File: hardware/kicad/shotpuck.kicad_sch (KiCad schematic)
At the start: 27 parts, among them J1 Magnetic pogo 2P (female), J2 TC2030-NL, Q1 DMN63D8LDW, U1 MDBT50Q-512K, U2 LIS2DE12TR, U3 MCP73831T-2ACI/OT

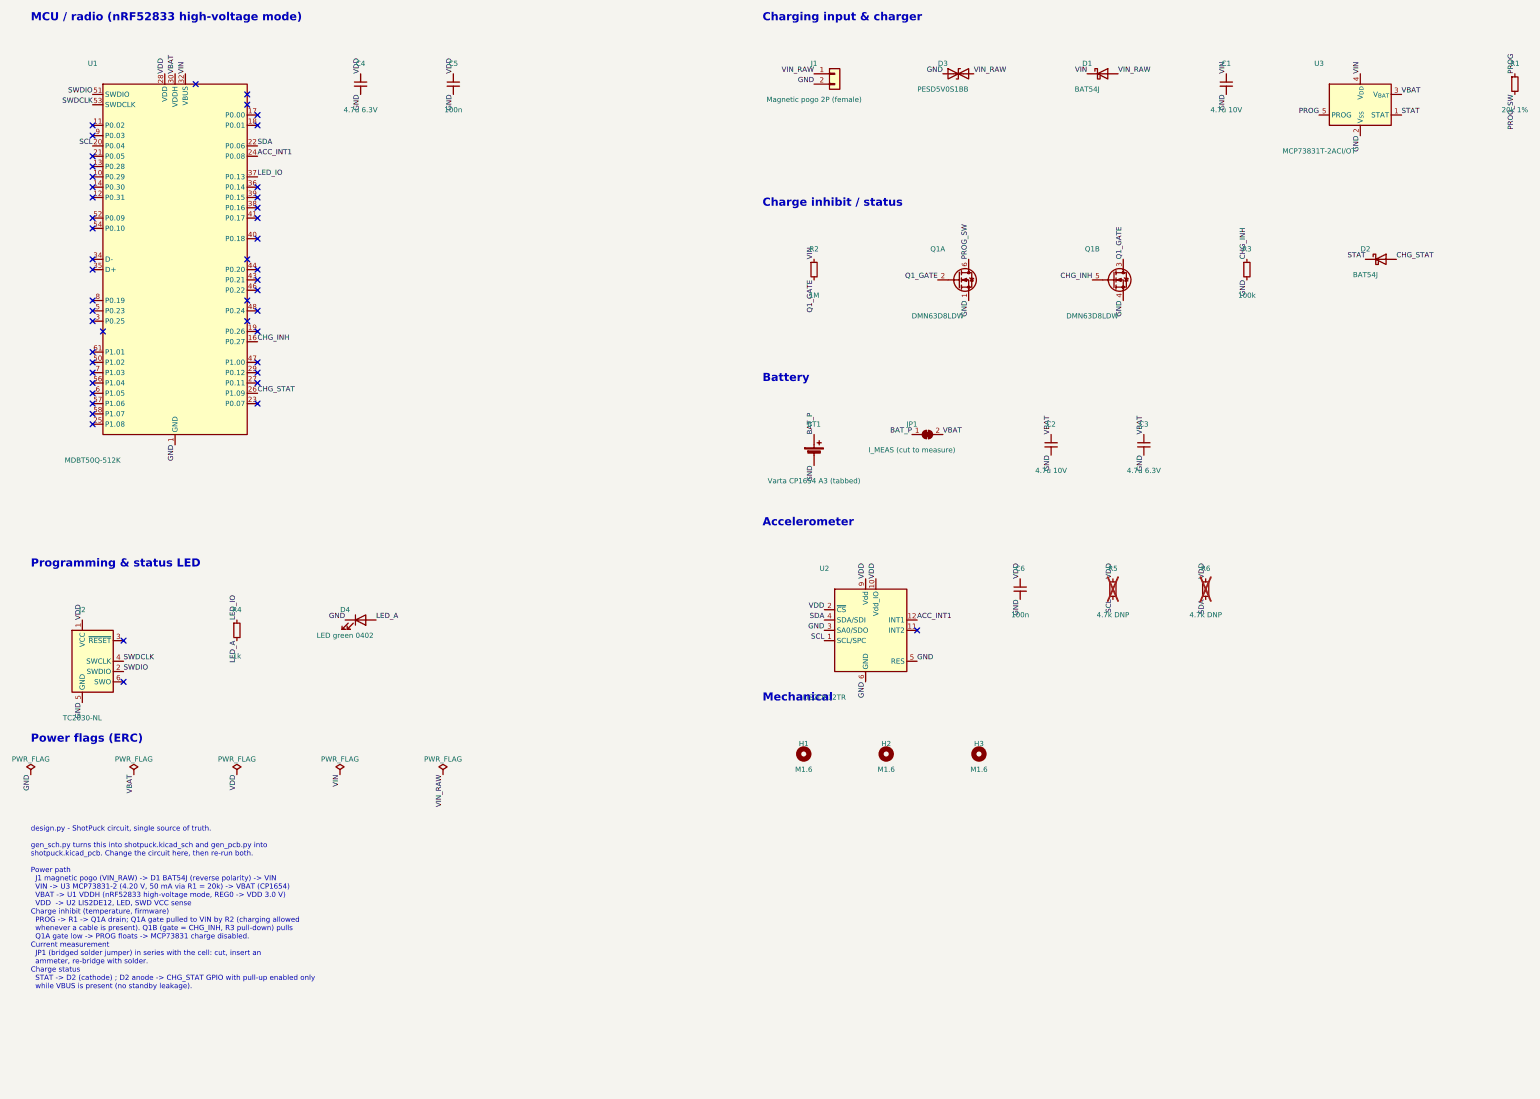
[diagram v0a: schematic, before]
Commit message: Update ShotPuck to v0.2 design package
Enhancements include the integration of the LSM6DSO32 IMU, which replaces the LIS2DE12 accelerometer, allowing for 6-axis motion capture. The new CAPTURE characteristic streams raw data around each shot, improving performance metrics. The firmware and simulation have been updated to support these changes, including adjustments to the BLE protocol (v2) for better data handling. Additionally, the toolchain has been migrated to a native Windows environment for development.

Key changes:
- Updated deliverable status to v0.2.
- Added capture functionality for bow motion.
- Adjusted simulation and validation processes to reflect new hardware capabilities.
- Enhanced documentation to include new features and user requirements.

Co-Authored-By: Claude Opus 5.5 <noreply@anthropic.com>
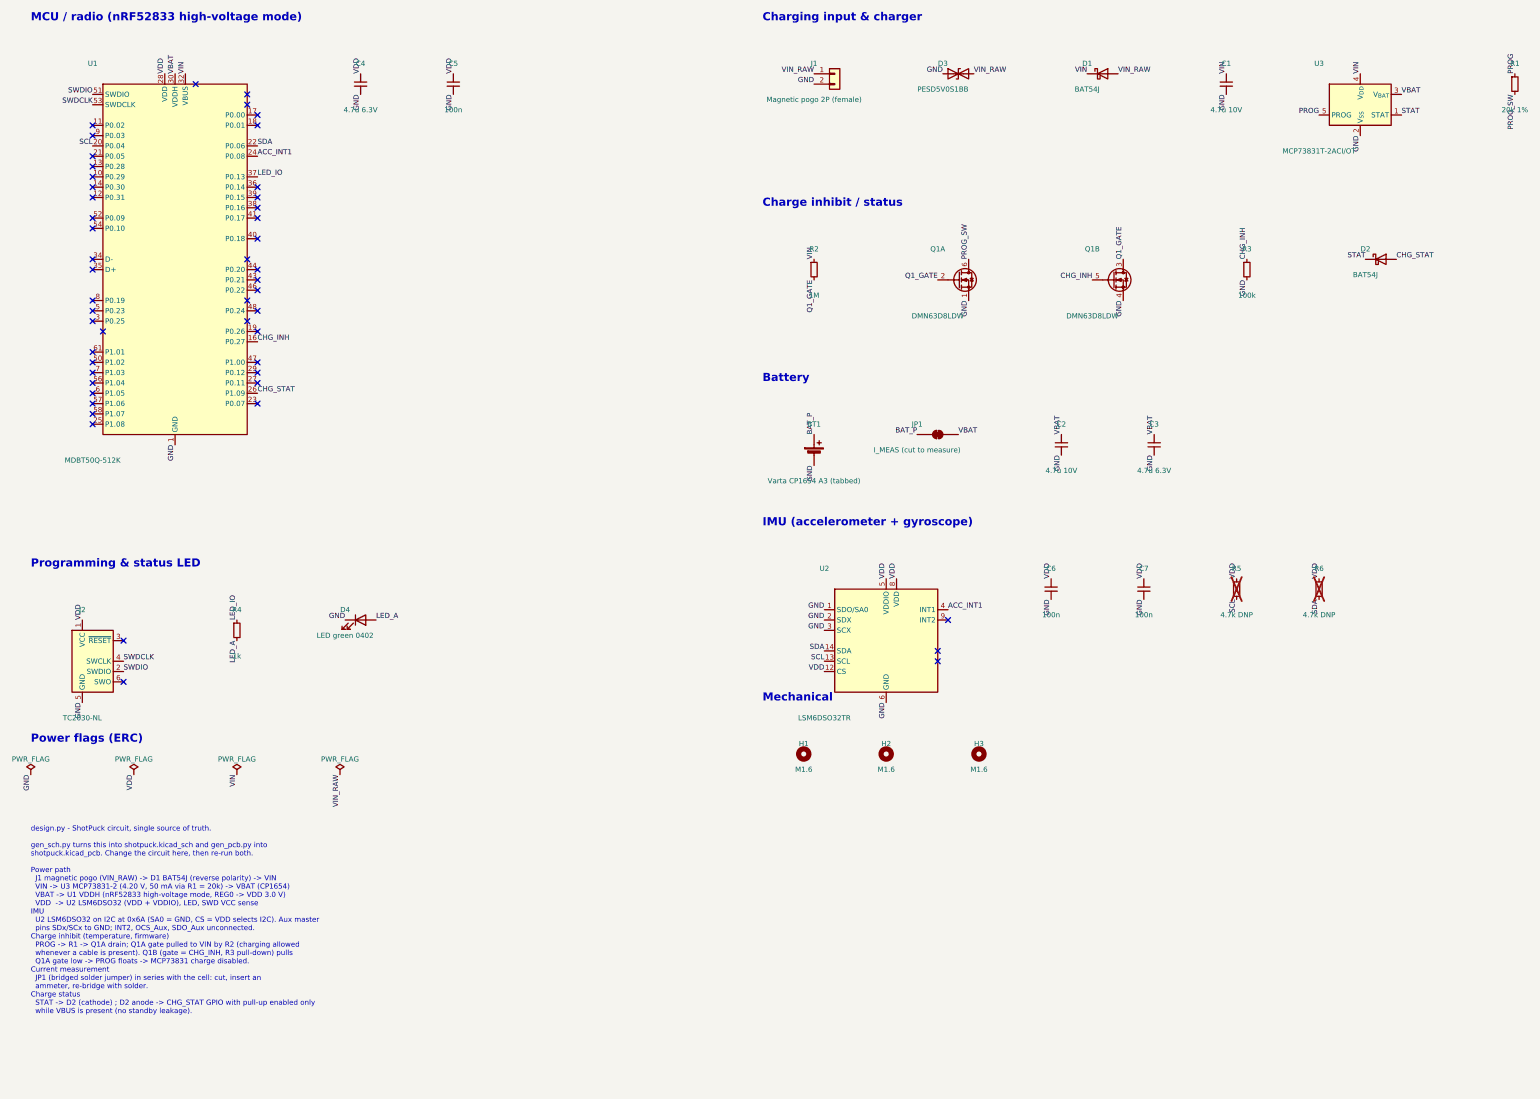
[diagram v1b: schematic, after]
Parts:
- added C7: 100n, Capacitor_SMD:C_0402_1005Metric, symbol Device:C_Small
- H1, H2, H3: footprint ShotPuck:MountingHole_1.8mm_M1.6 -> ShotPuck:MountingHole_1.8mm_NPTH
- Q1: symbol Device:Q_Dual_NMOS_S1G1D2S2G2D1 -> Transistor_FET:Q_Dual_NMOS_S1G1D2S2G2D1
- U2: value LIS2DE12TR -> LSM6DSO32TR; footprint Package_LGA:LGA-12_2x2mm_P0.5mm -> Package_LGA:LGA-14_3x2.5mm_P0.5mm_LayoutBorder3x4y; symbol Sensor_Motion:LIS2DE12 -> Sensor_Motion:LSM6DSL
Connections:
- net ACC_INT1: now also U2.4 (INT1); no longer U2.12 (INT1)
- net GND: now also U2.1 (SDO/SA0), U2.2 (SDX), C7.2; no longer U2.5 (RES), U2.8 (GND)
- net SCL: now also U2.13 (SCL); no longer U2.1 (SCL/SPC)
- net SDA: now also U2.14 (SDA); no longer U2.4 (SDA/SDI)
- net VDD: now also U2.12 (CS), U2.5 (VDDIO), U2.8 (VDD), C7.1; no longer U2.10 (Vdd_IO), U2.2 (~{CS}), U2.9 (Vdd)
- no-connect marks 48 -> 50
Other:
- note added: "IMU (accelerometer + gyroscope)"
- note removed: "Accelerometer"
- moved on the sheet: C2, C3, C6, R5, R6

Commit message: Add OTA, nRF52840, PCM, magnetic connector, Ø36 board and JLC panel
- Firmware: nRF52840 module (MDBT50Q-1MV2), MCUboot swap-using-move with
  ECDSA-P256 signed images, MCUmgr SMP over encrypted BLE, watchdog and
  self-confirm; 1 MB flash layout; release images shotpuck_full.hex and
  shotpuck_update.bin (v0.2.0).
- Hardware: BQ29700 + DMN2004DWK cell protection, universal CP1654 pads,
  Samzo magnetic 2-pin connector, Ø36 mm board inside the Ø40 mm puck,
  0.3 mm vias, 2x2 KiKit panel and JLCPCB BOM/CPL (gen_panel.py, gen_jlc.py).
- Mechanical: cavity sized for Varta CP1654 swell, connector chimney,
  optional brass Ø8 trim pins (balance reported with and without them).
- gen_pcb.py: stitching after all routing, connectivity rebuilt before fills,
  pre-routed Q2 drain and Q1 GND links, Freerouting optimizer off, up to 4
  board attempts until nothing is unconnected. DRC 0/0, panel DRC 0/0.

Co-Authored-By: Claude Opus 5.5 <noreply@anthropic.com>
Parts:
- added C8: 100n, Capacitor_SMD:C_0402_1005Metric, symbol Device:C_Small
- added Q2: DMN2004DWK, Package_TO_SOT_SMD:SOT-363_SC-70-6, symbol Transistor_FET:Q_Dual_NMOS_S1G1D2S2G2D1
- added R7: 330R, Resistor_SMD:R_0402_1005Metric, symbol Device:R_Small
- added R8: 2.2k, Resistor_SMD:R_0402_1005Metric, symbol Device:R_Small
- added U4: BQ29700DSER, Package_SON:WSON-6_1.5x1.5mm_P0.5mm, symbol Battery_Management:BQ297xy
- BT1: value Varta CP1654 A3 (tabbed) -> Varta CP1654 A3 (wire or tag version); footprint ShotPuck:CP1654_Tabbed -> ShotPuck:CP1654_Pads
- J1: value Magnetic pogo 2P (female) -> Samzo PR5L4015-2P-C-F; footprint ShotPuck:MagPogo_2P -> ShotPuck:MagPogo_Samzo_2P
- U1: value MDBT50Q-512K -> MDBT50Q-1MV2; symbol RF_Module:MDBT50Q-512K -> RF_Module:MDBT50Q-1MV2
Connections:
- net GND: now also Q2.4 (S), R8.2; no longer BT1.2 (-)
- net VBAT: now also R7.1
- new net BAT_N: BT1.2 (-), C8.2, Q2.1 (S), U4.4 (VSS)
- new net PCM_BAT: C8.1, R7.2, U4.5 (BAT)
- new net PCM_COUT: Q2.5 (G), U4.2 (Cout)
- new net PCM_D: Q2.3 (D), Q2.6 (D)
- new net PCM_DOUT: Q2.2 (G), U4.3 (Dout)
- new net PCM_VM: R8.1, U4.6 (V-)
- no-connect marks 50 -> 51
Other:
- note added: "Battery + protection (PCM)"
- note added: "MCU / radio (nRF52840 high-voltage mode)"
- note added: "design.py - ShotPuck circuit, single source of truth. gen_sch.py turns this into shotpuck.kicad_sch and gen_pcb.py into shotpuck.kicad_pcb. Change the circuit here, then re-run both. Power path J1 Samzo PR5L4015 magnetic receptacle (VIN_RAW) -> D1 BAT54J (reverse polarity) -> VIN VIN -> U3 MCP73831-2 (4.20 V, 50 mA via R1 = 20k) -> VBAT (CP1654) VBAT -> U1 VDDH (nRF52840 high-voltage mode, REG0 -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"
- note removed: "Battery"
- note removed: "MCU / radio (nRF52833 high-voltage mode)"
- note removed: "design.py - ShotPuck circuit, single source of truth. gen_sch.py turns this into shotpuck.kicad_sch and gen_pcb.py into shotpuck.kicad_pcb. Change the circuit here, then re-run both. Power path J1 magnetic pogo (VIN_RAW) -> D1 BAT54J (reverse polarity) -> VIN VIN -> U3 MCP73831-2 (4.20 V, 50 mA via R1 = 20k) -> VBAT (CP1654) VBAT -> U1 VDDH (nRF52833 high-voltage mode, REG0 -> VDD 3.0 V) VDD -> U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"

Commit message: Update ShotPuck design to rev A: replace stud with flat plate, adjust dimensions, and enhance PCB layout
- Redesigned the ShotPuck to use a 2.0 mm flat 6061 plate, bolted through a steel sleeve, improving manufacturability and cost.
- Adjusted dimensions: puck height reduced to 9.90 mm, with a center of mass 0.85 mm off-axis.
- Updated layout.json to reflect new design parameters, including cell placement and PCB notch.
- Enhanced mechanical and electrical design files, including updated battery specifications (LIR1254) and revised component placements.
- Improved documentation in HANDOVER.md and README.md to reflect changes in design and functionality.

Co-Authored-By: Claude Opus 5.5 <noreply@anthropic.com>
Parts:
- removed R5, R6: 4.7k DNP, Resistor_SMD:R_0402_1005Metric, symbol Device:R_Small
- BT1: value Varta CP1654 A3 (wire or tag version) -> LIR1254 (plain, spring contacts); footprint ShotPuck:CP1654_Pads -> ShotPuck:LIR1254_Contacts
- H1, H2, H3: value M1.6 -> M2; footprint ShotPuck:MountingHole_1.8mm_NPTH -> ShotPuck:MountingHole_2.4mm_NPTH
- J2: value TC2030-NL -> SWD pads; footprint Connector:Tag-Connect_TC2030-IDC-NL_2x03_P1.27mm_Vertical -> ShotPuck:SWD_Pads_1x4_P2.54; symbol Connector:Conn_ARM_SWD_TagConnect_TC2030-NL -> Connector_Generic:Conn_01x04
- R1: value 20k 1% -> 47k 1%
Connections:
- net GND: now also J2.4 (Pin_4); no longer J2.5 (GND)
- net SCL: now also U1.22 (P0.06); no longer U1.20 (P0.04)
- net SDA: now also U1.20 (P0.04); no longer U1.22 (P0.06)
- net SWDCLK: now also J2.3 (Pin_3); no longer J2.4 (SWCLK)
- no-connect marks 51 -> 49
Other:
- note added: "design.py - ShotPuck circuit, single source of truth. gen_sch.py turns this into shotpuck.kicad_sch and gen_pcb.py into shotpuck.kicad_pcb. Change the circuit here, then re-run both. Power path J1 Samzo PR5L4015 magnetic receptacle (VIN_RAW) -> D1 BAT54J (reverse polarity) -> VIN VIN -> U3 MCP73831-2 (4.20 V, 21 mA via R1 = 47k) -> VBAT (LIR1254, 45-65 mAh) VBAT -> U1 VDDH (nRF52840 high-voltage 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"
- note removed: "design.py - ShotPuck circuit, single source of truth. gen_sch.py turns this into shotpuck.kicad_sch and gen_pcb.py into shotpuck.kicad_pcb. Change the circuit here, then re-run both. Power path J1 Samzo PR5L4015 magnetic receptacle (VIN_RAW) -> D1 BAT54J (reverse polarity) -> VIN VIN -> U3 MCP73831-2 (4.20 V, 50 mA via R1 = 20k) -> VBAT (CP1654) VBAT -> U1 VDDH (nRF52840 high-voltage mode, REG0 -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"
- moved on the sheet: D4, R4
